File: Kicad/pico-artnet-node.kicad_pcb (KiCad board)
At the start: 2 copper layers, 100 x 100 mm, 28 parts, among them J1 Conn_01x03_Pin, J2 Conn_01x03_Pin, J3 Conn_01x04_Pin, J4 Conn_01x05_Pin, J5 Conn_01x05_Pin, J6 Conn_01x02_Socket, J7 Conn_01x02_Socket, SW1 SW_SPST, SW2 SW_SPST, SW3 SW_SPST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

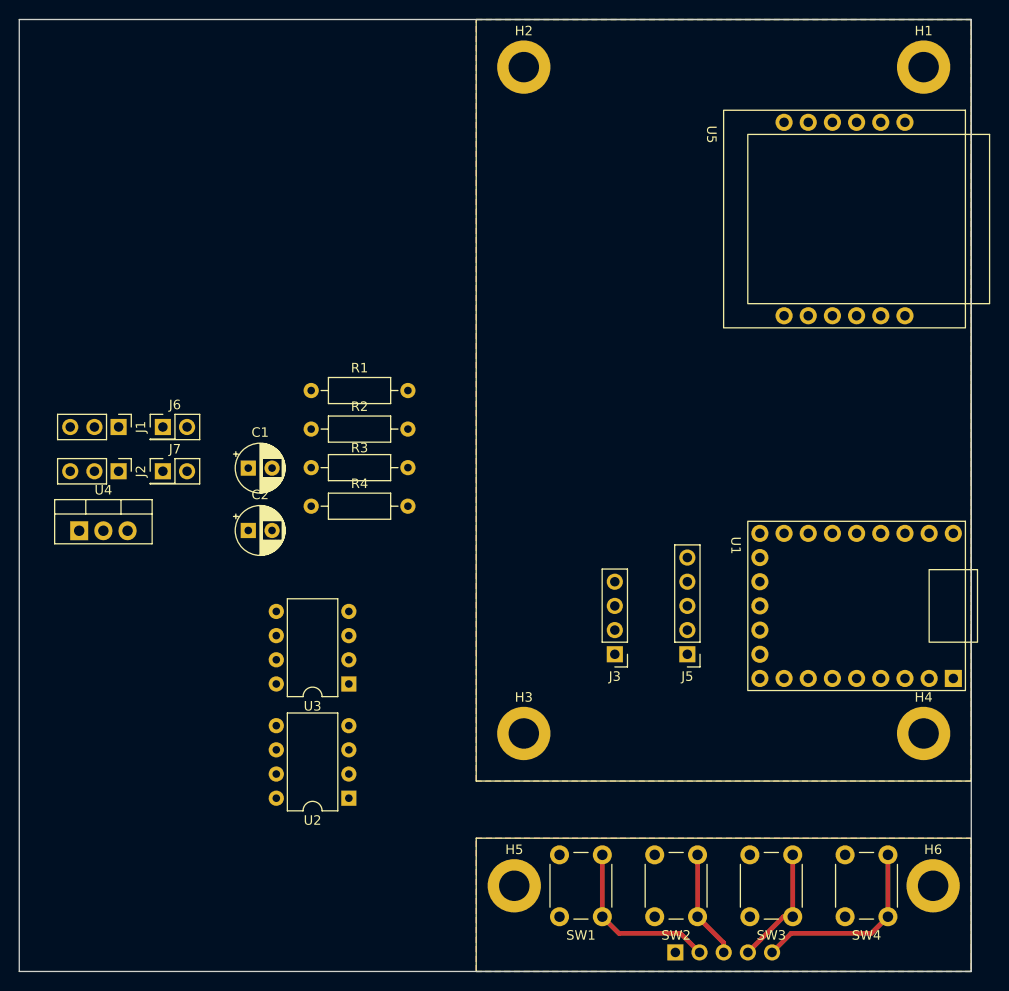
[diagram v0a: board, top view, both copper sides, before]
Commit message: swapped tx and led pins for better pcb layout
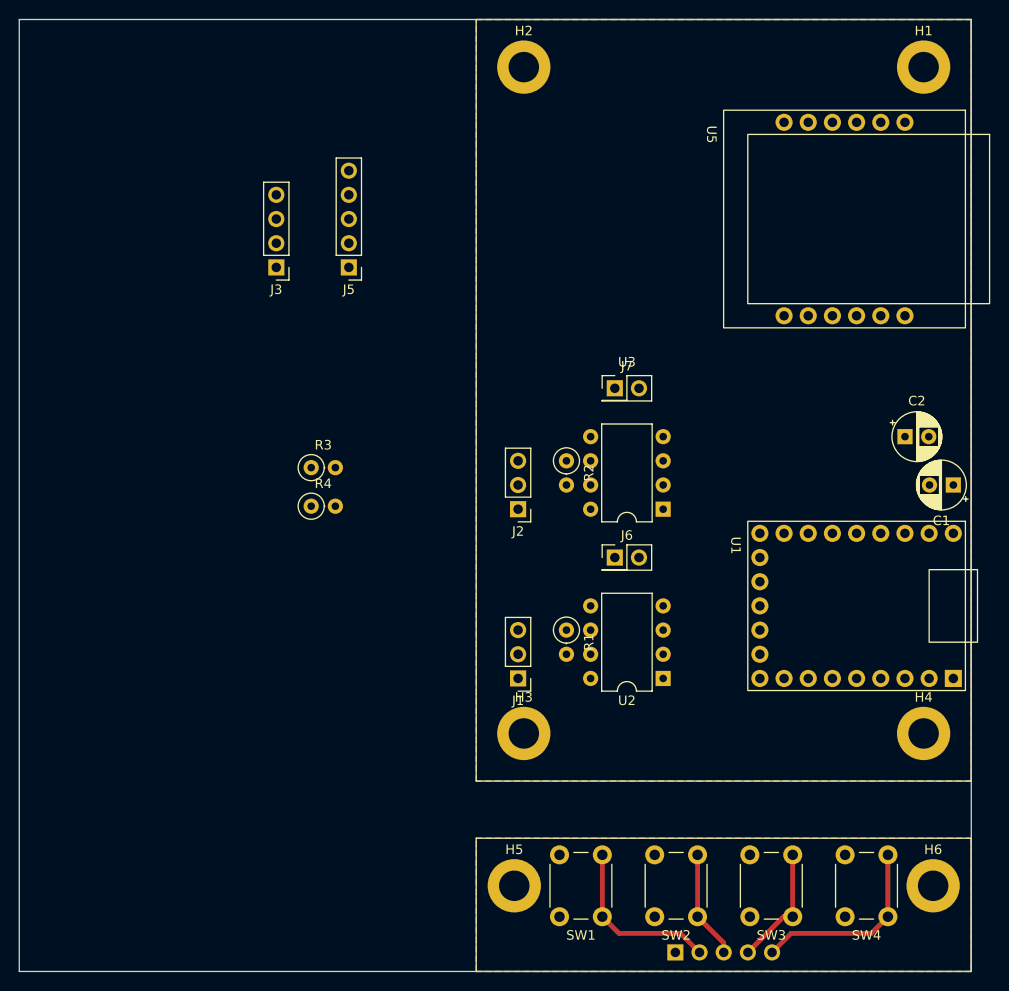
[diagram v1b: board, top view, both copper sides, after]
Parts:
- removed U4: LM1117DT-3.3, Package_TO_SOT_THT:TO-220-3_Vertical
- R1, R2, R3, R4: footprint Resistor_THT:R_Axial_DIN0207_L6.3mm_D2.5mm_P10.16mm_Horizontal -> Resistor_THT:R_Axial_DIN0207_L6.3mm_D2.5mm_P2.54mm_Vertical
- moved C1 74.1 mm to (198.1, 88.9), turned to 180 degrees
- moved C2 69.7 mm to (193.0, 83.8)
- moved J3 54.0 mm to (127.0, 66.0)
- moved J5 54.0 mm to (134.6, 66.0)
- moved J1 49.6 mm to (152.4, 109.2), turned to 180 degrees
- moved J6 49.4 mm to (162.6, 96.5)
- moved J7 48.3 mm to (162.6, 78.7)
- moved J2 42.2 mm to (152.4, 91.4), turned to 180 degrees
- moved U3 37.8 mm to (167.6, 91.4)
- moved R1 36.8 mm to (157.5, 104.1), turned to -90 degrees
- moved U2 35.3 mm to (167.6, 109.2)
- moved R2 27.0 mm to (157.5, 86.4), turned to -90 degrees
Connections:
- U1 pad 2: PORT_B_LED -> PORT_B_TX
- U1 pad 3: PORT_B_TX -> PORT_B_LED
- U1 pad 6: PORT_A_LED -> PORT_A_TX
- U1 pad 7: PORT_A_TX -> PORT_A_LED

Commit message: finished pcb
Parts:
- added SYM2: Logo_Open_Hardware_Small, Symbol:OSHW-Logo2_14.6x12mm_SilkScreen, F.Cu at (160.1, 59.7)
- moved J3 52.4 mm to (175.3, 86.4)
- moved J5 50.0 mm to (180.3, 86.4)
- moved J1 27.9 mm to (152.4, 81.3), turned to 0 degrees
- moved R3 26.6 mm to (154.9, 76.2)
- moved R4 24.9 mm to (154.9, 96.5)
- moved R1 20.3 mm to (157.5, 83.8)
- moved J6 20.3 mm to (162.6, 76.2)
- moved U2 20.3 mm to (167.6, 88.9)
- moved J7 17.8 mm to (162.6, 96.5)
- moved R2 17.8 mm to (157.5, 104.1)
- moved U3 17.8 mm to (167.6, 109.2)
- moved J2 10.2 mm to (152.4, 101.6), turned to 0 degrees
- moved C2 3.59 mm to (190.5, 86.4)
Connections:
- R1 pad 1: Net-(J1-Pin_3) -> Net-(J1-Pin_2)
- R1 pad 2: Net-(J1-Pin_2) -> Net-(J1-Pin_3)
- R2 pad 1: Net-(J2-Pin_3) -> Net-(J2-Pin_2)
- R2 pad 2: Net-(J2-Pin_2) -> Net-(J2-Pin_3)
- U2 pad 6: Net-(J1-Pin_3) -> Net-(J1-Pin_2)
- U2 pad 7: Net-(J1-Pin_2) -> Net-(J1-Pin_3)
- U3 pad 6: Net-(J2-Pin_3) -> Net-(J2-Pin_2)
- U3 pad 7: Net-(J2-Pin_2) -> Net-(J2-Pin_3)
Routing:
- net +5V: track 0.00 -> 71.2 mm
- net ETH_CS: track 0.00 -> 58.1 mm
- net ETH_INT: track 0.00 -> 49.3 mm
- net PORT_A_LED: track 0.00 -> 46.7 mm
- net ETH_SCK: track 0.00 -> 45.3 mm
- net ETH_MOSI: track 0.00 -> 45.0 mm
- net ETH_MISO: track 0.00 -> 44.1 mm
- net PORT_A_DIR: track 0.00 -> 43.9 mm
- net PORT_A_TX: track 0.00 -> 42.0 mm
- net PORT_A_RX: track 0.00 -> 40.7 mm
- net PORT_B_LED: track 0.00 -> 38.1 mm
- net PORT_B_DIR: track 0.00 -> 36.6 mm
- net PORT_B_RX: track 0.00 -> 34.0 mm
- net PORT_B_TX: track 0.00 -> 33.2 mm
- net DISPLAY_SCL: track 0.00 -> 31.3 mm
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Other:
- board size 100 x 100 mm -> 52 x 100 mm
- board text added: "Buttons"
- board text added: "DMX A"
- board text added: "DMX B"
- board text added: "Display"
- board text added: "E D U M"
- board text added: "JLCJLCJLCJLC"
- board text added: "Led A"
- board text added: "Led B"
- board text added: "MAX485"
- board text added: "Pico Artnet Node"
- board text added: "W5500"
- board text added: "https://www.github.com/ tommie1236/pico-artnet-node"
- board text added: "rp2040-zero"
- board text added: "© Timo Oosterom 2025"

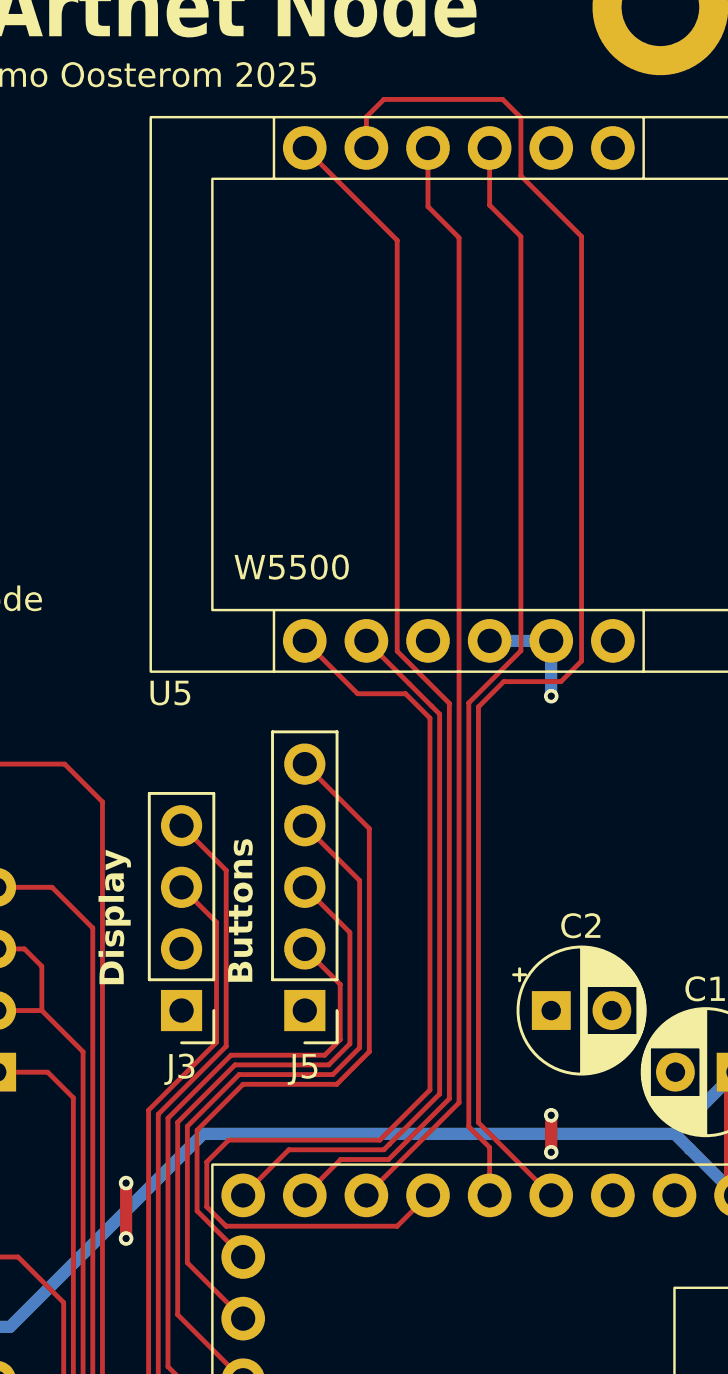
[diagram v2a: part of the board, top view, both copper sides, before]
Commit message: swapped miso and mosi lines so they connect correctly
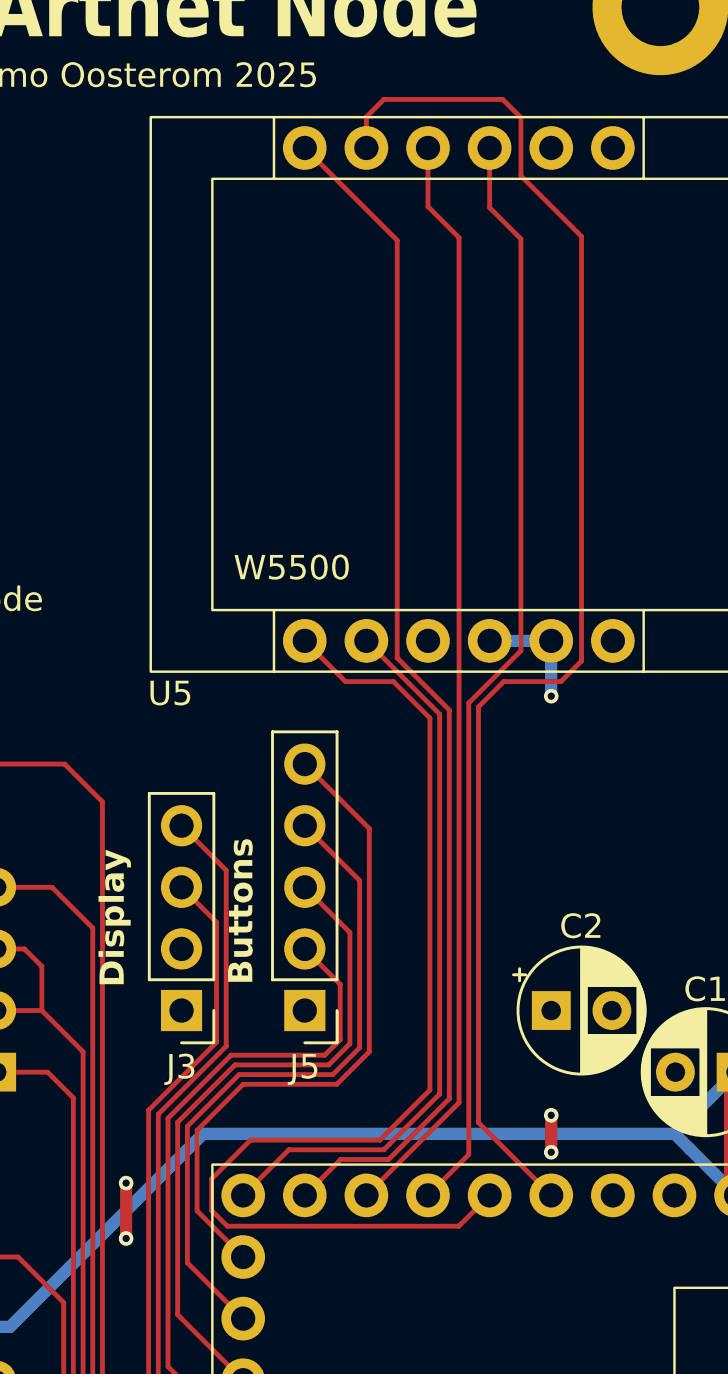
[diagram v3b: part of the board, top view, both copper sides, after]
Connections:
- U1 pad 17: ETH_MISO -> ETH_MOSI
- U1 pad 18: ETH_MOSI -> ETH_MISO
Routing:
- net ETH_MISO: track 44.1 -> 45.9 mm
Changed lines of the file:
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@@
 			)
 			(remove_unused_layers no)
-			(net 20 "ETH_MISO")
+			(net 26 "ETH_MOSI")
 			(pinfunction "GPIO_27")
 			(pintype "bidirectional")
@@
 			)
 			(remove_unused_layers no)
-			(net 26 "ETH_MOSI")
+			(net 20 "ETH_MISO")
 			(pinfunction "GPIO_28")
 			(pintype "bidirectional")
@@
 	)
 	(segment
-		(start 186.3 89.994314)
-		(end 186.3 73.697057)
+		(start 184.15 54.61)
+		(end 180.34 50.8)
 		(width 0.2)
 		(layer "F.Cu")
@@
 	)
 	(segment
-		(start 183.794314 92.5)
-		(end 186.3 89.994314)
+		(start 181.82 92.5)
+		(end 183.794314 92.5)
 		(width 0.2)
 		(layer "F.Cu")
@@
 	)
 	(segment
-		(start 184.15 54.61)
-		(end 180.34 50.8)
+		(start 183.794314 92.5)
+		(end 186.3 89.994314)
 		(width 0.2)
 		(layer "F.Cu")
@@
 	)
 	(segment
-		(start 181.82 92.5)
-		(end 183.794314 92.5)
+		(start 186.3 89.994314)
+		(end 186.3 73.974315)
 		(width 0.2)
 		(layer "F.Cu")
@@
 	)
 	(segment
-		(start 184.15 71.547057)
+		(start 184.15 71.824315)
 		(end 184.15 54.61)
 		(width 0.2)
@@
 	)
 	(segment
-		(start 186.3 73.697057)
-		(end 184.15 71.547057)
+		(start 186.3 73.974315)
+		(end 184.15 71.824315)
 		(width 0.2)
 		(layer "F.Cu")
@@
 	)
 	(segment
-		(start 183.434314 91.7)
-		(end 185.5 89.634314)
+		(start 177.15 95.25)
+		(end 176.5 94.6)
 		(width 0.2)
 		(layer "F.Cu")
@@
 	)
 	(segment
-		(start 182.52 73.3)
-		(end 180.34 71.12)
+		(start 185.5 89.634313)
+		(end 185.5 74.305686)
 		(width 0.2)
 		(layer "F.Cu")
@@
 	)
 	(segment
-		(start 185.5 89.634314)
-		(end 185.5 74.305686)
+		(start 182.02 72.8)
+		(end 180.34 71.12)
 		(width 0.2)
 		(layer "F.Cu")
@@
 	)
 	(segment
-		(start 185.5 74.305686)
-		(end 184.494314 73.3)
+		(start 183.434313 91.7)
+		(end 185.5 89.634313)
 		(width 0.2)
 		(layer "F.Cu")
@@
 	)
 	(segment
-		(start 184.15 95.25)
-		(end 177.095686 95.25)
+		(start 176.5 94.6)
+		(end 176.5 93.3)
 		(width 0.2)
 		(layer "F.Cu")
@@
 	)
 	(segment
-		(start 185.42 93.98)
-		(end 184.15 95.25)
+		(start 186.69 95.25)
+		(end 177.15 95.25)
 		(width 0.2)
 		(layer "F.Cu")
@@
 	)
 	(segment
-		(start 176.3 94.454314)
-		(end 176.3 92.6)
+		(start 183.994314 72.8)
+		(end 182.02 72.8)
 		(width 0.2)
 		(layer "F.Cu")
@@
 	)
 	(segment
-		(start 177.2 91.7)
-		(end 183.434314 91.7)
+		(start 178.1 91.7)
+		(end 183.434313 91.7)
 		(width 0.2)
 		(layer "F.Cu")
@@
 	)
 	(segment
-		(start 177.095686 95.25)
-		(end 176.3 94.454314)
+		(start 176.5 93.3)
+		(end 178.1 91.7)
 		(width 0.2)
 		(layer "F.Cu")
@@
 	)
 	(segment
-		(start 184.494314 73.3)
-		(end 182.52 73.3)
+		(start 187.96 93.98)
+		(end 186.69 95.25)
 		(width 0.2)
 		(layer "F.Cu")
@@
 	)
 	(segment
-		(start 176.3 92.6)
-		(end 177.2 91.7)
+		(start 185.5 74.305686)
+		(end 183.994314 72.8)
 		(width 0.2)
 		(layer "F.Cu")
@@
 	)
 	(segment
-		(start 187.1 91.145686)
-		(end 187.96 92.005686)
-		(width 0.2)
-		(layer "F.Cu")
-		(net 26)
-	)
-	(segment
-		(start 187.96 53.16)
-		(end 189.25 54.45)
+		(start 187.1 73.677057)
+		(end 189.25 71.527057)
 		(width 0.2)
 		(layer "F.Cu")
@@
 	(segment
 		(start 189.25 71.527057)
-		(end 187.1 73.677057)
+		(end 189.25 54.55)
 		(width 0.2)
 		(layer "F.Cu")
@@
 	)
 	(segment
-		(start 189.25 54.45)
-		(end 189.25 71.527057)
+		(start 189.25 54.55)
+		(end 187.96 53.26)
 		(width 0.2)
 		(layer "F.Cu")
@@
 	)
 	(segment
-		(start 187.96 92.005686)
-		(end 187.96 93.98)
+		(start 187.96 53.26)
+		(end 187.96 50.8)
 		(width 0.2)
 		(layer "F.Cu")
@@
 	)
 	(segment
-		(start 187.1 73.677057)
-		(end 187.1 91.145686)
+		(start 187.1 92.3)
+		(end 187.1 73.677057)
 		(width 0.2)
 		(layer "F.Cu")
@@
 	)
 	(segment
-		(start 187.96 50.8)
-		(end 187.96 53.16)
+		(start 185.42 93.98)
+		(end 187.1 92.3)
 		(width 0.2)
 		(layer "F.Cu")
